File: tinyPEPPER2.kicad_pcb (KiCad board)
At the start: 4 copper layers, 20 x 20 mm, 165 parts, among them T201 BC847, T202 BC847, T203 BC847, T301 BC847, T302 BC847, T303 BC847, T401 BC847, T402 BC847, T403 BC847, T501 BC847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

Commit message: minor cleanup of traces
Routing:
- net GND: track 230.4 -> 231.2 mm
- net /single esc 2/Bp_0: track 5.53 -> 4.92 mm

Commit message: added docs
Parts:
- U1: footprint TO_SOT_Packages_SMD:SOT-23-5 -> custom:SOT-23-5
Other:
- board text added: "C2CK 1"
- board text added: "C2CK 2"
- board text added: "C2CK 3"
- board text added: "C2CK 4"
- board text added: "GND -"
- board text added: "RC IN / RX 2"
- board text added: "RX 3 / RC IN"
- board text added: "VCC +"
- board text removed: "RC IN / RX 3"
- board text removed: "RX 2 / RC IN"

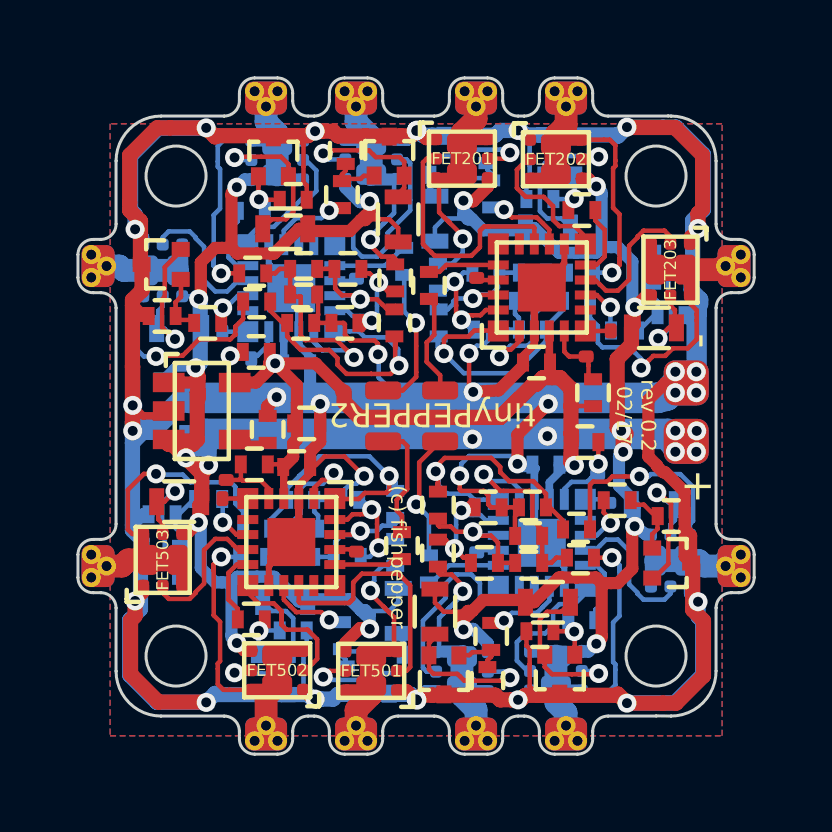
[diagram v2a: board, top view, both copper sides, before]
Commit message: fixed npn T
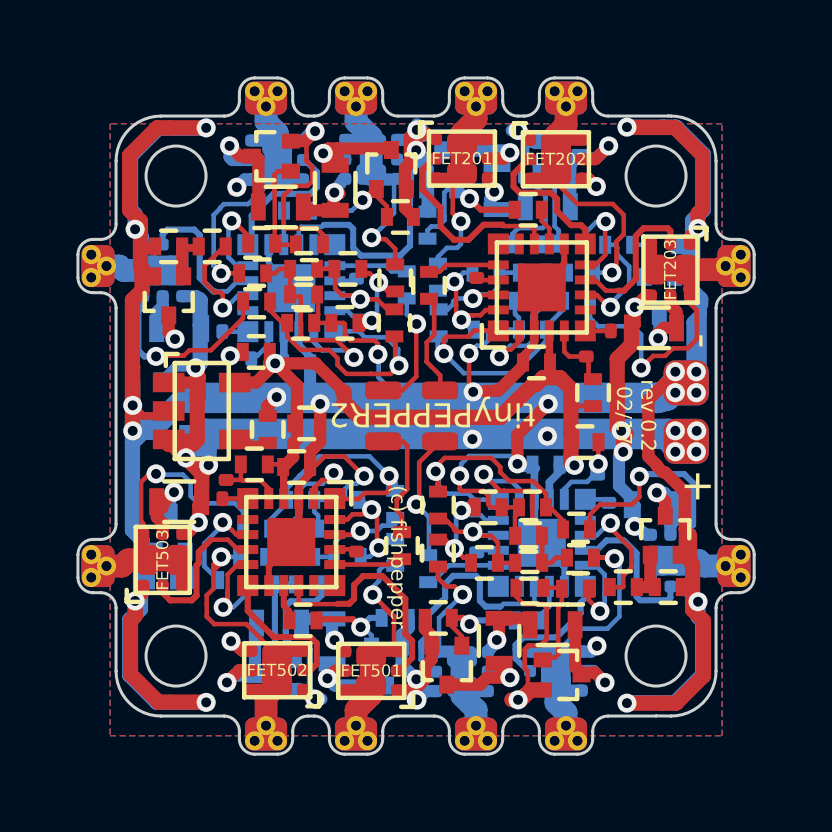
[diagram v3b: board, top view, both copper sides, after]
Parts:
- R211, R312, R412, R511: moved to F.Cu
- R212, R311, R411, R512: moved to B.Cu
- moved R217 3.21 mm to (110.4, 103.6)
- moved R413 2.90 mm to (116.9, 115.7)
- moved R317 2.87 mm to (109.5, 103.4), turned to 180 degrees
- moved R213 2.86 mm to (116.8, 104.3)
- moved R513 2.71 mm to (103.0, 115.5)
- moved R417 2.66 mm to (110.7, 116.7), turned to 0 degrees
- moved R517 2.65 mm to (109.3, 116.7), turned to 180 degrees
- moved R313 2.55 mm to (103.2, 104.3)
- moved R514 2.43 mm to (107.2, 117.5)
- moved R419 2.37 mm to (118.4, 115.7)
- moved R414 2.35 mm to (112.8, 117.5)
- moved R219 2.35 mm to (118.3, 104.3)
- moved R314 2.35 mm to (107.3, 102.4)
- moved R319 2.33 mm to (101.8, 104.3)
- moved R214 2.32 mm to (112.7, 102.4)
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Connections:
- T201 pad 2: Net-(FET201-Pad5) -> GND
- T201 pad 3: GND -> Net-(FET201-Pad5)
- T202 pad 2: Net-(FET202-Pad5) -> GND
- T202 pad 3: GND -> Net-(FET202-Pad5)
- T203 pad 2: Net-(FET203-Pad5) -> GND
- T203 pad 3: GND -> Net-(FET203-Pad5)
- T301 pad 2: Net-(FET301-Pad5) -> GND
- T301 pad 3: GND -> Net-(FET301-Pad5)
- T302 pad 2: Net-(FET302-Pad5) -> GND
- T302 pad 3: GND -> Net-(FET302-Pad5)
- T303 pad 2: Net-(FET303-Pad5) -> GND
- T303 pad 3: GND -> Net-(FET303-Pad5)
- T401 pad 2: Net-(FET401-Pad5) -> GND
- T401 pad 3: GND -> Net-(FET401-Pad5)
- T402 pad 2: Net-(FET402-Pad5) -> GND
- T402 pad 3: GND -> Net-(FET402-Pad5)
- T403 pad 2: Net-(FET403-Pad5) -> GND
- T403 pad 3: GND -> Net-(FET403-Pad5)
- T501 pad 2: Net-(FET501-Pad5) -> GND
- T501 pad 3: GND -> Net-(FET501-Pad5)
- T502 pad 2: Net-(FET502-Pad5) -> GND
- T502 pad 3: GND -> Net-(FET502-Pad5)
- T503 pad 2: Net-(FET503-Pad5) -> GND
- T503 pad 3: GND -> Net-(FET503-Pad5)
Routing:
- net VCC: track 127.4 -> 81.7 mm, vias 23 -> 22
- net GND: track 231.2 -> 223.4 mm, vias 31 -> 32
- net Net-(R211-Pad1): track 1.87 -> 4.58 mm, vias 0 -> 1
- net Net-(R413-Pad2): track 1.86 -> 4.04 mm
- net Net-(R313-Pad2): track 1.61 -> 3.74 mm
- net Net-(R213-Pad2): track 1.94 -> 3.85 mm
- net Net-(FET501-Pad5): track 5.29 -> 3.53 mm
- net Net-(FET402-Pad5): track 5.46 -> 3.71 mm
- net Net-(R311-Pad1): track 1.87 -> 3.60 mm, vias 0 -> 1
- net Net-(R511-Pad1): track 1.87 -> 3.55 mm, vias 0 -> 1
- net Net-(FET203-Pad5): track 5.25 -> 3.58 mm
- net Net-(FET502-Pad5): track 5.46 -> 3.85 mm
- net /single esc 2/Ap_0: track 7.96 -> 9.57 mm
- net Net-(FET302-Pad5): track 5.46 -> 3.88 mm
- net Net-(R411-Pad1): track 1.87 -> 3.30 mm, vias 0 -> 1
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
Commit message: new pads
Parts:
- removed TP11, TP13: TP, custom:TP_powerpad
- TP10, TP12: footprint custom:TP_powerpad -> custom:TP_POWER_PAD_DOUBLESIDED
- moved TP10 0.08 mm to (119.1, 110.8)
- moved TP12 0.07 mm to (119.1, 108.9)
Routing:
- net VCC: vias 22 -> 18
- net GND: vias 32 -> 28
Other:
- board text added: "rev 0.3 03/17"
- board text removed: "rev 0.2 02/17"

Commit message: fixing sch
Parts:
- C1000: value 47u -> 22u
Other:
- board text added: "RC / RX 1"
- board text added: "RC / RX 2"
- board text added: "RC / RX 3"
- board text added: "RC / RX 4"
- board text added: "rev 0.4 04/18"
- board text removed: "RC IN / RX 1"
- board text removed: "RC IN / RX 2"
- board text removed: "RX 3 / RC IN"
- board text removed: "RX 4 / RC IN"
- board text removed: "rev 0.3 03/17"
